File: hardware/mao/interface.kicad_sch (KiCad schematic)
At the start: 27 parts, among them J301 LCD, J302 TOUCH TOP, J303 TOUCH REAR, Q301 AO3400A, SW301 SKQGADE010, U301 DRV5012AEDMRR, U302 DRV5012AEDMRR

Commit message: hardware: MAO_MAIN A0 routed board, fab package and final review
6-layer JLC06161H-3313 board (F / GND / signals / +3V3 / GND / B), routed from the
design scripts: designed power and fan-out copper, grid router with closed-set A*,
stub pruning, GND stitching (two ties on large pour fragments), tidy.
DRC 0 violations / 0 unconnected / 0 parity; ERC 0; silkscreen checker 0 findings.

- silkscreen: ODD JOBS mark and identity on both faces, S/N box, function-named
  test pads in a 3.0 x 3.2 mm service field; references for every semiconductor and
  connector plus the passives the service docs name, the rest on assembly drawings
- stackup, black mask, white legend and ENIG written into the board
- fab: 6-layer Gerbers + drill, JLC BOM (47 lines, LCSC on every line) and CPL
  (113 parts), assembly PDFs, FAB-NOTES with computed via counts
- docs: PCB, ODD JOBS and order-readiness review sections, final report, renders,
  factory-test pad map, bring-up and architecture updates

Co-Authored-By: Claude Opus 5.5 <noreply@anthropic.com>
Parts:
- R301, R302: LCSC (none) -> C25092; MPN (none) -> 0402WGF220JTCE; Manufacturer (none) -> UNI-ROYAL
- R303: LCSC (none) -> C22859; MPN (none) -> 0603WAF100JT5E; Manufacturer (none) -> UNI-ROYAL
- R304: LCSC (none) -> C25076; MPN (none) -> 0402WGF1000TCE; Manufacturer (none) -> UNI-ROYAL
- R307, R308, R309, R310: LCSC (none) -> C25123; MPN (none) -> 0402WGF5100TCE; Manufacturer (none) -> UNI-ROYAL
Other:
- note added: "ALPS SKQG on F.Cu at the centre, under"
- note added: "EC11 (2 transitions per detent, 30 detents). HALL_FAST low = 20 Hz sampling, 1.6 uA (sleep); high = 2.5 kHz (awake)."
- note added: "GPIO0 = BOOT strap: no capacitor here."
- note added: "Two DRV5012 Hall latches under the 30-pole magnet ring, 6 deg apart (half a pole = 90 deg electrical): A/B quadrature identical to the LCDkit"
- note added: "the panel: the floating face presses it."
- note removed: "ALPS SKQG on B.Cu at the centre: the"
- note removed: "LCDkit EC11 (2 transitions per detent, 30 detents). HALL_FAST low = 20 Hz sampling, 1.6 uA (sleep); high = 2.5 kHz (awake)."
- note removed: "Two DRV5012 Hall latches under the 30-pole magnet ring, 30 deg apart (2.5 pole pitches = 90 deg electrical): A/B quadrature identical to the"
- note removed: "strap: no capacitor here."
- note removed: "whole top unit presses it. GPIO0 = BOOT"
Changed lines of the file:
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@@
 			)
 		)
-		(property "MPN" ""
+		(property "MPN" "0402WGF220JTCE"
 			(at 68.58 31.75 0)
 			(effects
@@
 			)
 		)
-		(property "Manufacturer" ""
+		(property "Manufacturer" "UNI-ROYAL"
 			(at 68.58 31.75 0)
 			(effects
@@
 			)
 		)
-		(property "LCSC" ""
+		(property "LCSC" "C25092"
 			(at 68.58 31.75 0)
 			(effects
@@
 			)
 		)
-		(property "MPN" ""
+		(property "MPN" "0402WGF220JTCE"
 			(at 105.41 31.75 0)
 			(effects
@@
 			)
 		)
-		(property "Manufacturer" ""
+		(property "Manufacturer" "UNI-ROYAL"
 			(at 105.41 31.75 0)
 			(effects
@@
 			)
 		)
-		(property "LCSC" ""
+		(property "LCSC" "C25092"
 			(at 105.41 31.75 0)
 			(effects
@@
 			)
 		)
-		(property "MPN" ""
+		(property "MPN" "0603WAF100JT5E"
 			(at 172.72 31.75 0)
 			(effects
@@
 			)
 		)
-		(property "Manufacturer" ""
+		(property "Manufacturer" "UNI-ROYAL"
 			(at 172.72 31.75 0)
 			(effects
@@
 			)
 		)
-		(property "LCSC" ""
+		(property "LCSC" "C22859"
 			(at 172.72 31.75 0)
 			(effects
@@
 			)
 		)
-		(property "MPN" ""
+		(property "MPN" "0402WGF1000TCE"
 			(at 237.49 31.75 0)
 			(effects
@@
 			)
 		)
-		(property "Manufacturer" ""
+		(property "Manufacturer" "UNI-ROYAL"
 			(at 237.49 31.75 0)
 			(effects
@@
 			)
 		)
-		(property "LCSC" ""
+		(property "LCSC" "C25076"
 			(at 237.49 31.75 0)
 			(effects
@@
 		)
 	)
-	(text "Two DRV5012 Hall latches under the 30-pole magnet ring, 30 deg apart (2.5 pole pitches = 90 deg electrical): A/B quadrature identical to the"
+	(text "Two DRV5012 Hall latches under the 30-pole magnet ring, 6 deg apart (half a pole = 90 deg electrical): A/B quadrature identical to the LCDkit"
 		(exclude_from_sim no)
 		(at 15.24 170.18 0)
@@
 		)
 	)
-	(text "LCDkit EC11 (2 transitions per detent, 30 detents). HALL_FAST low = 20 Hz sampling, 1.6 uA (sleep); high = 2.5 kHz (awake)."
+	(text "EC11 (2 transitions per detent, 30 detents). HALL_FAST low = 20 Hz sampling, 1.6 uA (sleep); high = 2.5 kHz (awake)."
 		(exclude_from_sim no)
 		(at 15.24 172.72 0)
@@
 		)
 	)
-	(text "ALPS SKQG on B.Cu at the centre: the"
+	(text "ALPS SKQG on F.Cu at the centre, under"
 		(exclude_from_sim no)
 		(at 160.02 121.92 0)
@@
 		)
 	)
-	(text "whole top unit presses it. GPIO0 = BOOT"
+	(text "the panel: the floating face presses it."
 		(exclude_from_sim no)
 		(at 160.02 123.19 0)
@@
 		)
 	)
-	(text "strap: no capacitor here."
+	(text "GPIO0 = BOOT strap: no capacitor here."
 		(exclude_from_sim no)
 		(at 160.02 125.73 0)
@@
 			)
 		)
-		(property "MPN" ""
+		(property "MPN" "0402WGF5100TCE"
 			(at 219.71 109.22 0)
 			(effects
@@
 			)
 		)
-		(property "Manufacturer" ""
+		(property "Manufacturer" "UNI-ROYAL"
 			(at 219.71 109.22 0)
 			(effects
@@
 			)
 		)
-		(property "LCSC" ""
+		(property "LCSC" "C25123"
 			(at 219.71 109.22 0)
 			(effects
@@
 			)
 		)
-		(property "MPN" ""
+		(property "MPN" "0402WGF5100TCE"
 			(at 283.21 109.22 0)
 			(effects
@@
 			)
 		)
-		(property "Manufacturer" ""
+		(property "Manufacturer" "UNI-ROYAL"
 			(at 283.21 109.22 0)
 			(effects
@@
 			)
 		)
-		(property "LCSC" ""
+		(property "LCSC" "C25123"
 			(at 283.21 109.22 0)
 			(effects
@@
 			)
 		)
-		(property "MPN" ""
+		(property "MPN" "0402WGF5100TCE"
 			(at 261.62 142.24 0)
 			(effects
@@
 			)
 		)
-		(property "Manufacturer" ""
+		(property "Manufacturer" "UNI-ROYAL"
 			(at 261.62 142.24 0)
 			(effects
@@
 			)
 		)
-		(property "LCSC" ""
+		(property "LCSC" "C25123"
 			(at 261.62 142.24 0)
 			(effects
@@
 			)
 		)
-		(property "MPN" ""
+		(property "MPN" "0402WGF5100TCE"
 			(at 321.31 142.24 0)
 			(effects
@@
 			)
 		)
-		(property "Manufacturer" ""
+		(property "Manufacturer" "UNI-ROYAL"
 			(at 321.31 142.24 0)
 			(effects
@@
 			)
 		)
-		(property "LCSC" ""
+		(property "LCSC" "C25123"
 			(at 321.31 142.24 0)
 			(effects

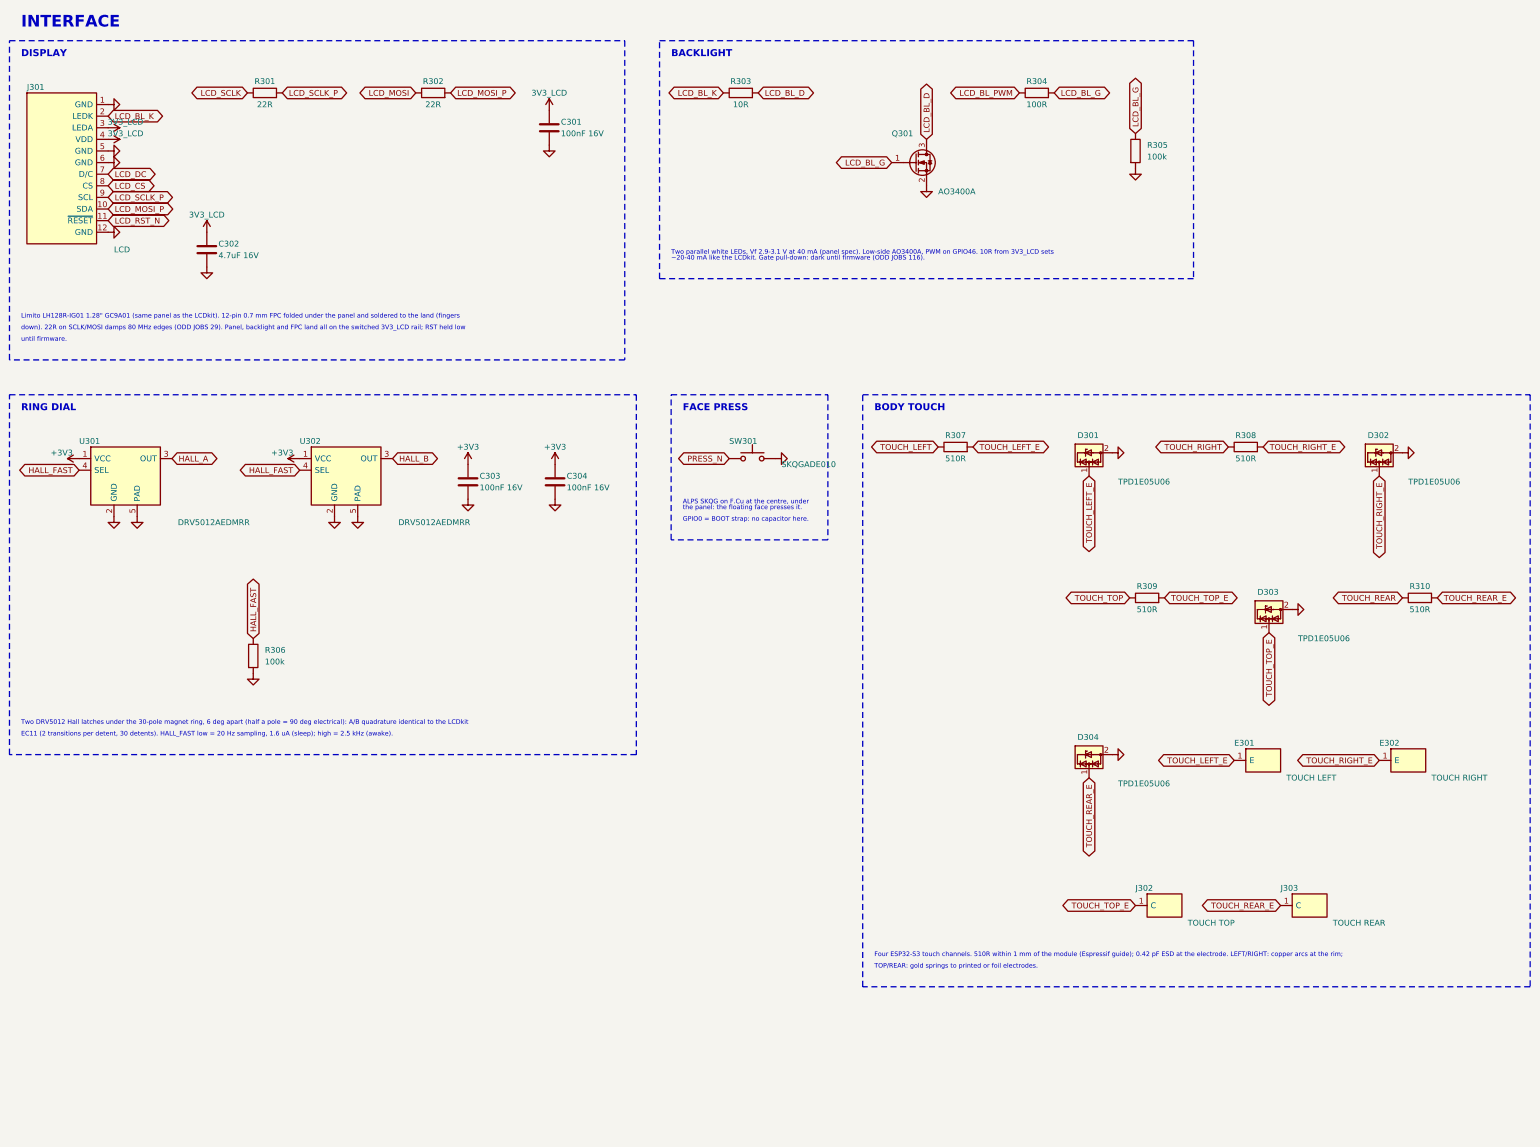
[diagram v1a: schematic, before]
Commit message: hardware: MAO_MAIN A0 4-layer release, plug-in display, ODD JOBS review
- 4 layers (JLC04161H-1080): L1 parts + critical lines, L2 solid GND,
  L3 power regions + slow lines, L4 parts + lines. Re-placed and
  re-routed from scratch: 191 vias (6-layer board: 230).
- J301 HDGC 0.5K-HX-18PWB (C2919497): the round panel plugs in, no
  solder (Winstar 18-pin standard); display TE line added.
- 4-layer pin map; firmware header, pin-map doc and schematic notes
  generated from pinmap.py.
- Pipeline steps: power_regions, plane_check, via_off_pad, snap45 (all
  segments 0/45/90), models3d (datasheet-height bodies for every part).
- Checks: DRC/ERC/parity 0, every L2/L3 plane one piece, silk checker 0,
  Gerbers reviewed independently, firmware 5 configs 0 warnings.
- Mechanical: display standoff 2.7 mm for IR-receiver clearance, ToF
  light-blocking gasket, mic gasket tube, TOP-spring boss; panel tabs at
  2 and 8 o'clock.
- Docs: 4-layer design review, 200-rule ODD JOBS compliance, final
  report, layer plots, Gerber sheet, renders.

Co-Authored-By: Claude Opus 5.5 <noreply@anthropic.com>
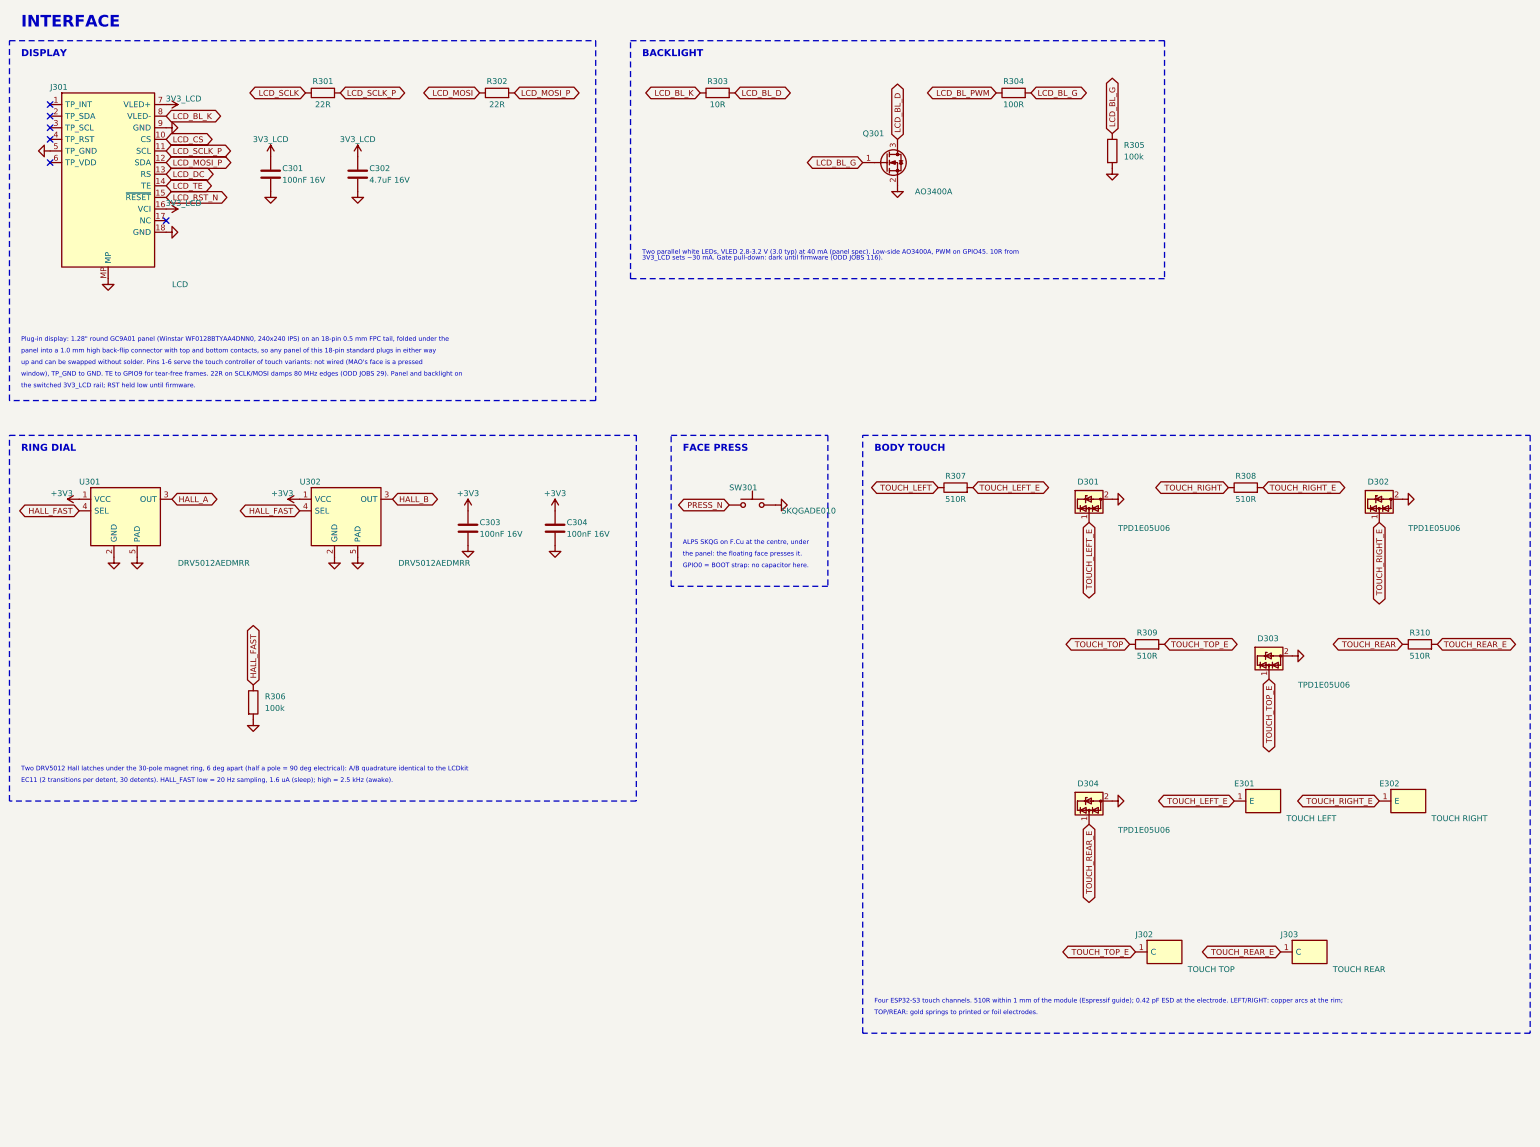
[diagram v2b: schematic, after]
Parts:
- J301: footprint MAO:Limito_LH128R_FPC_12P_P0.7mm_SolderLand -> MAO:HDGC_0.5K-HX-18PWB_1x18-1MP_P0.5mm_Horizontal; symbol MAO:LH128R_FPC -> MAO:ROUND_LCD_FPC18; Exclude from BOM yes -> (none); LCSC (none) -> C2919497; MPN PCB feature: LH128R-IG01 FPC land -> 0.5K-HX-18PWB; Manufacturer (none) -> HDGC; now in the parts list
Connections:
- net 3V3_LCD: now also J301.16 (VCI), J301.7 (VLED+); no longer J301.3 (LEDA), J301.4 (VDD)
- net GND: now also J301.18 (GND), J301.9 (GND), J301.MP; no longer J301.1 (GND), J301.12 (GND), J301.6 (GND)
- net LCD_BL_K: now also J301.8 (VLED-); no longer J301.2 (LEDK)
- net LCD_CS: now also J301.10 (CS); no longer J301.8 (CS)
- net LCD_DC: now also J301.13 (RS); no longer J301.7 (D/C)
- net LCD_MOSI_P: now also J301.12 (SDA); no longer J301.10 (SDA)
- net LCD_RST_N: now also J301.15 (~{RESET}); no longer J301.11 (~{RESET})
- net LCD_SCLK_P: now also J301.11 (SCL); no longer J301.9 (SCL)
- new net LCD_TE: J301.14 (TE)
- no-connect marks 0 -> 6
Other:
- note added: "3V3_LCD sets ~30 mA. Gate pull-down: dark until firmware (ODD JOBS 116)."
- note added: "Plug-in display: 1.28" round GC9A01 panel (Winstar WF0128BTYAA4DNN0, 240x240 IPS) on an 18-pin 0.5 mm FPC tail, folded under the"
- note added: "Two parallel white LEDs, VLED 2.8-3.2 V (3.0 typ) at 40 mA (panel spec). Low-side AO3400A, PWM on GPIO45. 10R from"
- note added: "panel into a 1.0 mm high back-flip connector with top and bottom contacts, so any panel of this 18-pin standard plugs in either way"
- note added: "the switched 3V3_LCD rail; RST held low until firmware."
- note added: "up and can be swapped without solder. Pins 1-6 serve the touch controller of touch variants: not wired (MAO's face is a pressed"
- note added: "window), TP_GND to GND. TE to GPIO9 for tear-free frames. 22R on SCLK/MOSI damps 80 MHz edges (ODD JOBS 29). Panel and backlight on"
- note removed: "Limito LH128R-IG01 1.28" GC9A01 (same panel as the LCDkit). 12-pin 0.7 mm FPC folded under the panel and soldered to the land (fingers"
- note removed: "Two parallel white LEDs, Vf 2.9-3.1 V at 40 mA (panel spec). Low-side AO3400A, PWM on GPIO46. 10R from 3V3_LCD sets"
- note removed: "down). 22R on SCLK/MOSI damps 80 MHz edges (ODD JOBS 29). Panel, backlight and FPC land all on the switched 3V3_LCD rail; RST held low"
- note removed: "until firmware."
- note removed: "~20-40 mA like the LCDkit. Gate pull-down: dark until firmware (ODD JOBS 116)."
- moved on the sheet: C301, C302, C303, C304, D301, D302, D303, D304, E301, E302, J302, J303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
